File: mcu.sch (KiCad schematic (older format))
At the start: 11 parts

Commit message: Update schematic to KEMET and Panasonic passives.
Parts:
- removed C? (x3): CAP-EIA0402, footprints_generic:CAPC100X50X55L30N, symbol gz_Ceramic-Capacitors:CAP-EIA0402
- removed R?: RES-EIA0402, footprints_generic:RESC100X50X40L25NN, symbol gz_Chip-Resistors-Surface-Mount:RES-EIA0402
- added C? (x3): CAP-EIA0402, footprints_generic:CAPC100X50X55L30N, symbol gz_Ceramic-Capacitors:CAP-EIA0402
- added R?: RES-EIA0402, footprints_generic:RESC100X50X40L25NN, symbol gz_Chip-Resistors-Surface-Mount:RES-EIA0402
- C?: Dielectric X7R -> X5R; Digi-Key_PN 490-13341-1-ND -> (none); Fit (none) -> Yes; MPN GRM155R71E104ME14D -> C0402C104K4PACTU; Manufacturer Murata Electronics -> KEMET; Tolerance ±20% -> ±10%; Vendor (none) -> Digikey; Vendor_PN (none) -> 399-7762-1-ND; Voltage 25V -> 16V
- R?: Digi-Key_PN 541-4011-1-ND -> (none); Fit (none) -> Yes; MPN CRCW0402100KJNEDC -> ERJ-2GEJ104X; Manufacturer Vishay Dale -> Panasonic Electronic Components; Power 1/16W -> 1/10W; Vendor (none) -> Digikey; Vendor_PN (none) -> P100KJCT-ND; Voltage 50V -> N/A
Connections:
- net FLASH_MISO_IO1: now also R?.1
- net GND: now also C?.2, C?.2, C?.2, R?.2
- net at U?.26 (VDD_SDIO): now also C?.1
- net at U?.19 (VDD3P3_RTC), U?.37 (VDD3P3_CPU): now also C?.1, C?.1

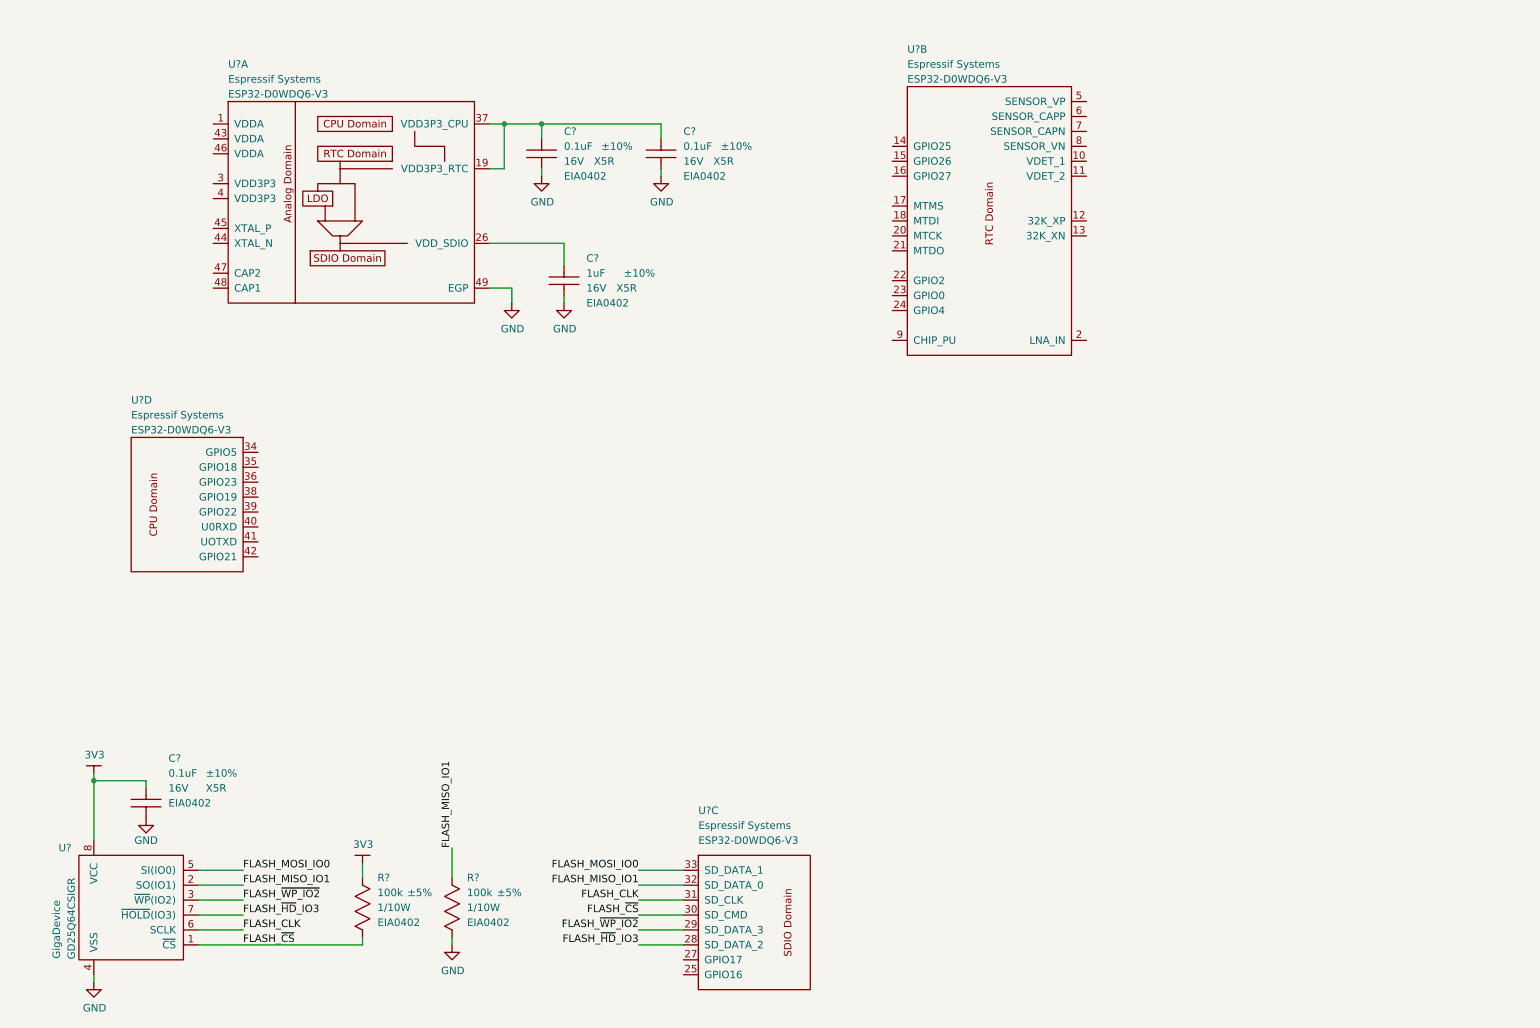
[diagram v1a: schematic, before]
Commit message: Add VDD3P3 pins decoupling and HF harmonics filter.
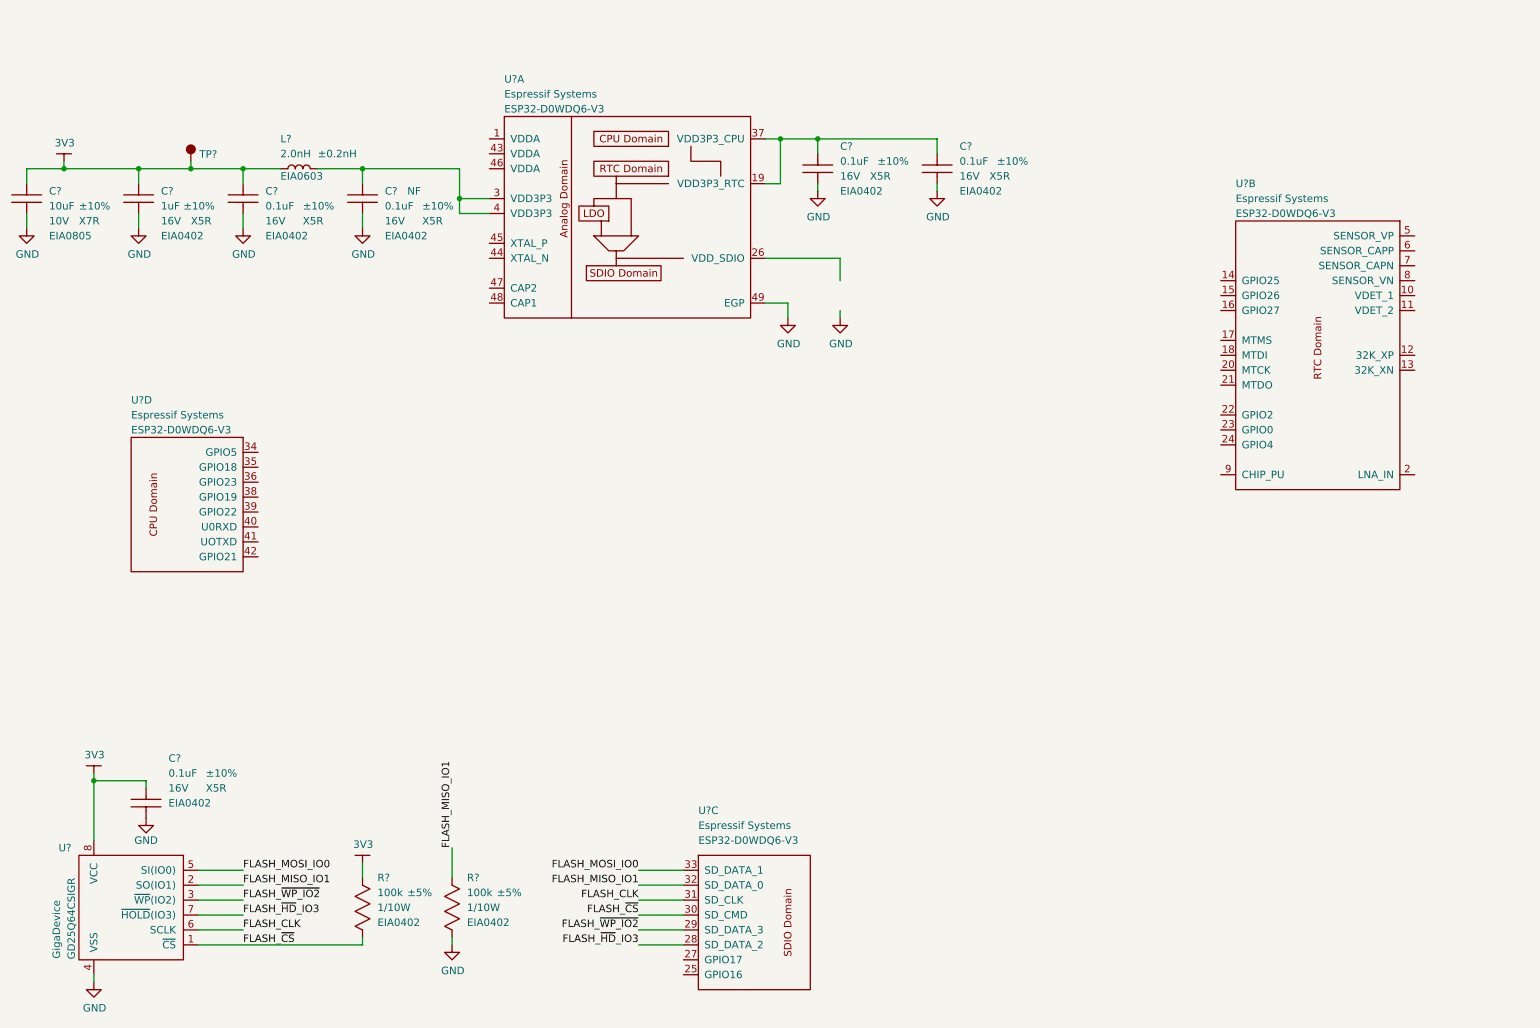
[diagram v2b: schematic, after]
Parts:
- added C? (x2): CAP-EIA0402, footprints_generic:CAPC100X50X55L30N, symbol gz_Ceramic-Capacitors:CAP-EIA0402
- added C?: CAP-EIA0805, footprints_generic:CAPC200X125X110L50N, symbol gz_Ceramic-Capacitors:CAP-EIA0805
- added L?: IND-EIA0603, footprints_generic:INDC160X80X95L40N, symbol gz_Fixed-Inductors:IND-EIA0603
- added TP?: Test-Point-SMT, footprints_generic:TestPoint-SMT_C100, symbol gz_Test-Points:Test-Point-SMT
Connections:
- wire segments 35 -> 56
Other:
- moved on the sheet: C?, U?A, U?B

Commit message: Sync repo, no change.
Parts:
- added C?: CAP-EIA0402, footprints_generic:CAPC100X50X55L30N, symbol gz_Ceramic-Capacitors:CAP-EIA0402
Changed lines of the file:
@@
-$Comp
-L gz_RF-Transceiver-ICs:Espressif_ESP32-D0WDQ6-V3 U?
-U 2 1 60500F62
-P 9350 2950
-F 0 "U?" H 8800 4000 50  0000 L CNN
-F 1 "Espressif_ESP32-D0WDQ6-V3" H 11100 4650 50  0001 L CNN
-F 2 "footprints:Espressif-ESP32_QFN49P40_600X600X90L40X20T430N" H 11100 4550 50  0001 L CNN
-F 3 "${DATASHEETS}/Espressif_ESP32-D0WDQ6-V3.pdf" H 10700 4250 50  0001 L CNN
-F 4 "1904-ESP32-D0WDQ6-V3CT-ND" H 11450 4450 50  0001 L CNN "Vendor_PN"
-F 5 "Espressif Systems" H 8800 3900 50  0000 L CNN "Manufacturer"
-F 6 "ESP32-D0WDQ6-V3" H 8800 3800 50  0000 L CNN "MPN"
-F 7 "RF/IF and RFID" H 11100 4350 50  0001 L CNN "Category"
-F 8 "RF Transceiver ICs" H 11100 4250 50  0001 L CNN "Family"
-F 9 "Yes" H 9100 3800 50  0001 L CNN "Fit"
-F 10 "Digikey" H 11100 4450 50  0001 L CNN "Vendor"
-	2    9350 2950
-	1    0    0    -1
-$EndComp
 $Comp
 L gz_RF-Transceiver-ICs:Espressif_ESP32-D0WDQ6-V3 U?
@@
 Wire Wire Line
 	1800 1800 1450 1800
+$Comp
+L gz_RF-Transceiver-ICs:Espressif_ESP32-D0WDQ6-V3 U?
+U 2 1 60500F62
+P 9350 2950
+F 0 "U?" H 8800 4000 50  0000 L CNN
+F 1 "Espressif_ESP32-D0WDQ6-V3" H 11100 4650 50  0001 L CNN
+F 2 "footprints:Espressif-ESP32_QFN49P40_600X600X90L40X20T430N" H 11100 4550 50  0001 L CNN
+F 3 "${DATASHEETS}/Espressif_ESP32-D0WDQ6-V3.pdf" H 10700 4250 50  0001 L CNN
+F 4 "1904-ESP32-D0WDQ6-V3CT-ND" H 11450 4450 50  0001 L CNN "Vendor_PN"
+F 5 "Espressif Systems" H 8800 3900 50  0000 L CNN "Manufacturer"
+F 6 "ESP32-D0WDQ6-V3" H 8800 3800 50  0000 L CNN "MPN"
+F 7 "RF/IF and RFID" H 11100 4350 50  0001 L CNN "Category"
+F 8 "RF Transceiver ICs" H 11100 4250 50  0001 L CNN "Family"
+F 9 "Yes" H 9100 3800 50  0001 L CNN "Fit"
+F 10 "Digikey" H 11100 4450 50  0001 L CNN "Vendor"
+	2    9350 2950
+	1    0    0    -1
+$EndComp
+$Comp
+L gz_Ceramic-Capacitors:CAP-EIA0402 C?
+U 1 1 60517A0C
+P 6150 2650
+F 0 "C?" V 6100 2800 50  0000 L CNN
+F 1 "CAP-EIA0402" H 6550 3750 50  0001 L CNN
+F 2 "footprints_generic:CAPC100X50X55L30N" H 2850 7000 50  0001 L CNN
+F 3 "${KEMET_MLCC_BASE}C0402C105K4PACTU" H 2850 7100 50  0001 L CNN
+F 4 "Digikey" H 6150 2650 50  0001 L CNN "Vendor"
+F 5 "399-12289-1-ND" H 6150 2650 50  0001 L CNN "Vendor_PN"
+F 6 "KEMET" H 6550 3550 50  0001 L CNN "Manufacturer"
+F 7 "C0402C105K4PACTU" H 6550 3450 50  0001 L CNN "MPN"
+F 8 "Capacitors" H 2850 7400 50  0001 L CNN "Category"
+F 9 "Ceramic Capacitors" H 2850 7500 50  0001 L CNN "Family"
+F 10 "Yes" H 6150 2650 50  0001 L CNN "Fit"
+F 11 "1uF" V 6200 2800 50  0000 L CNN "Capacitance"
+F 12 "±10%" V 6200 2950 50  0000 L CNN "Tolerance"
+F 13 "16V" V 6300 2800 50  0000 L CNN "Voltage"
+F 14 "X5R" V 6300 3000 50  0000 L CNN "Dielectric"
+F 15 "EIA0402" V 6400 2800 50  0000 L CNN "Package"
+	1    6150 2650
+	0    1    1    0
+$EndComp
 $EndSCHEMATC

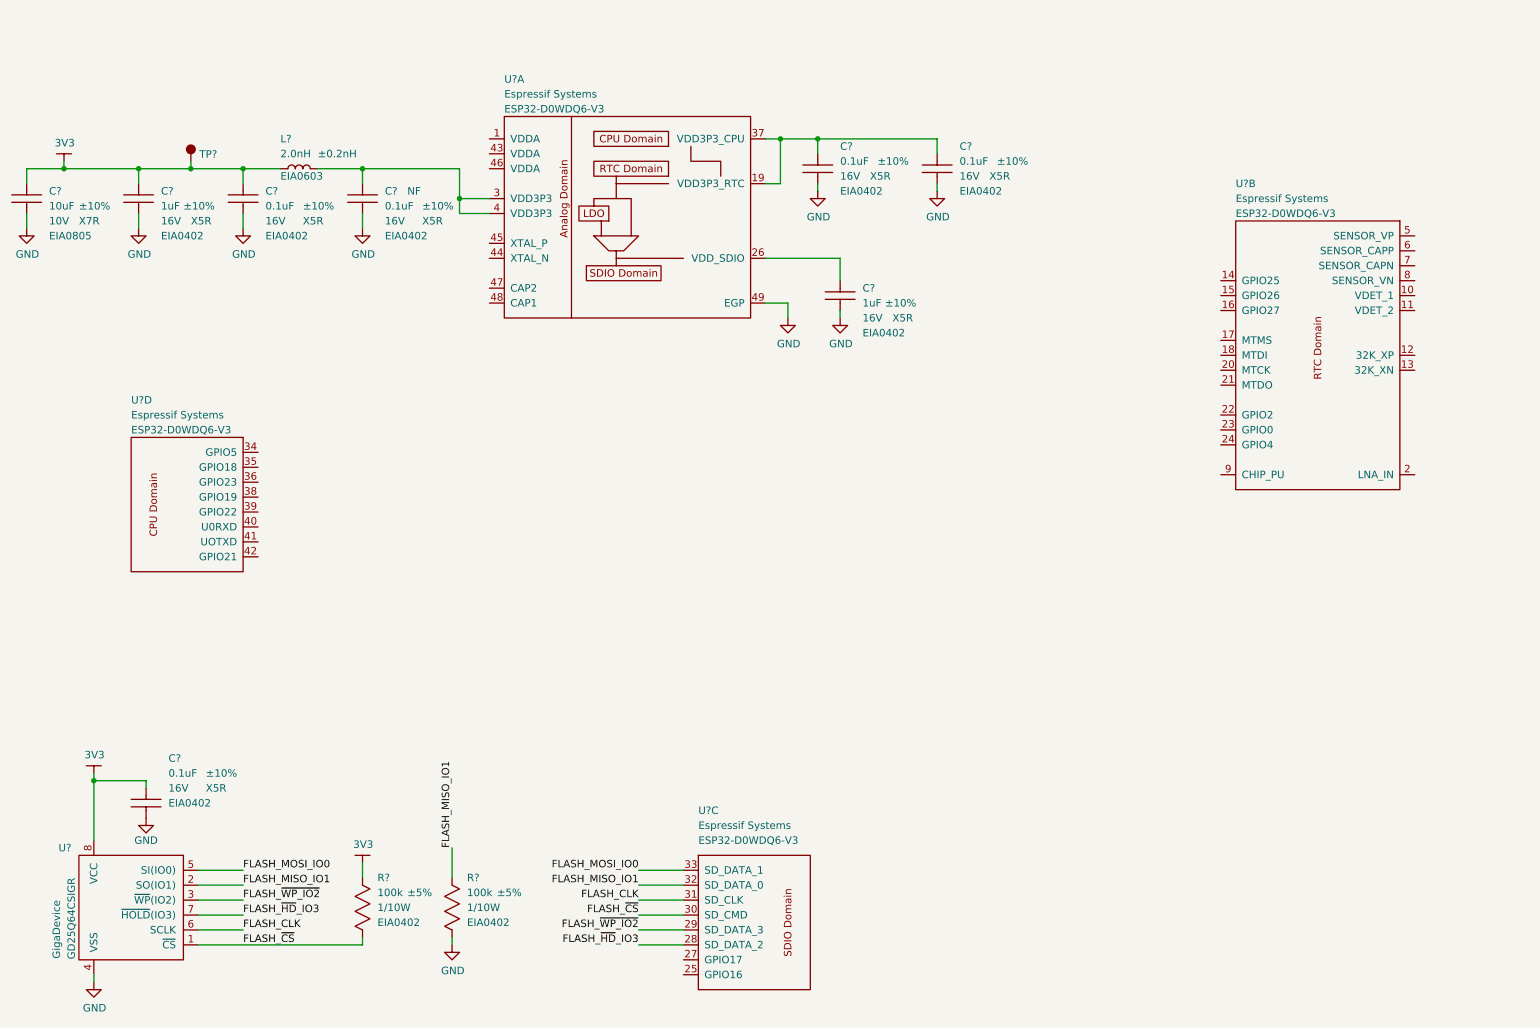
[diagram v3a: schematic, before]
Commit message: Conclude PSU section of ESP32.
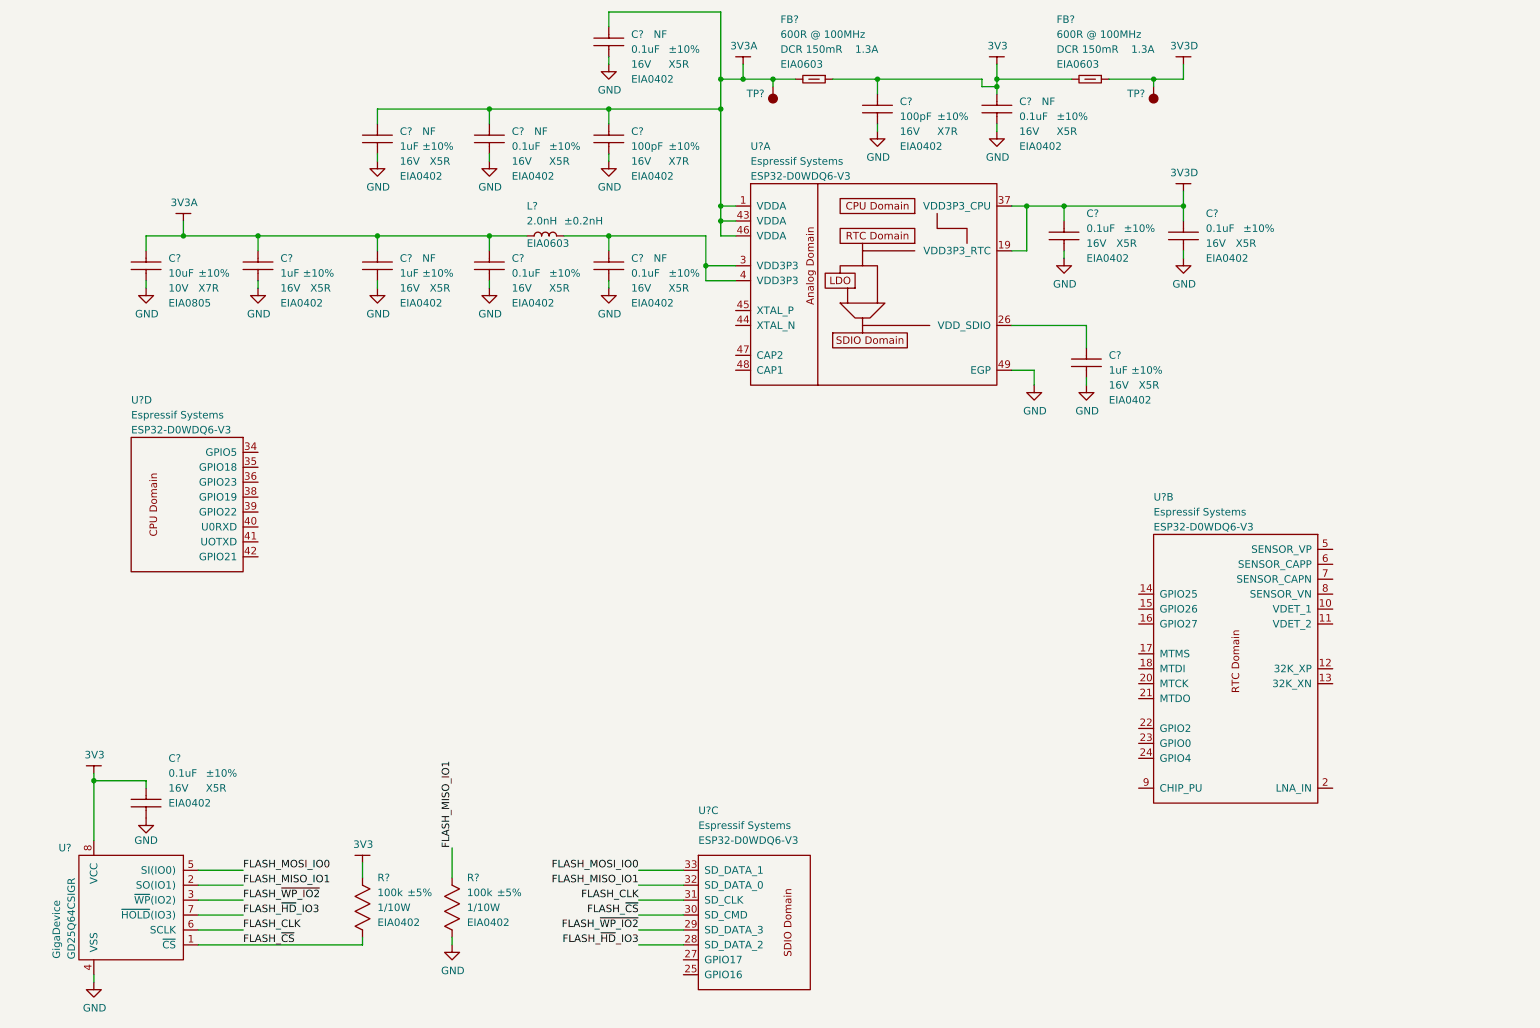
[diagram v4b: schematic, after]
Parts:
- added C? (x7): CAP-EIA0402, footprints_generic:CAPC100X50X55L30N, symbol gz_Ceramic-Capacitors:CAP-EIA0402
- added FB? (x2): FB-EIA0603, footprints_generic:BEADC160X80X95L40N, symbol gz_Ferrite-Beads-and-Chips:FB-EIA0603
- added TP?: Test-Point-SMT, footprints_generic:TestPoint-SMT_C100, symbol gz_Test-Points:Test-Point-SMT
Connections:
- net +3V3: now also C?.1, C?.1, U?.1 (VDDA), U?.19 (VDD3P3_RTC), U?.37 (VDD3P3_CPU), U?.43 (VDDA), U?.46 (VDDA), C?.1, C?.1, C?.1, C?.1, C?.1, C?.1, C?.1, FB?.1, FB?.1, FB?.2, FB?.2, TP?.1
- net GND: now also C?.2, C?.2, C?.2, C?.2, C?.2, C?.2, C?.2
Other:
- moved on the sheet: C?, L?, U?A, U?B

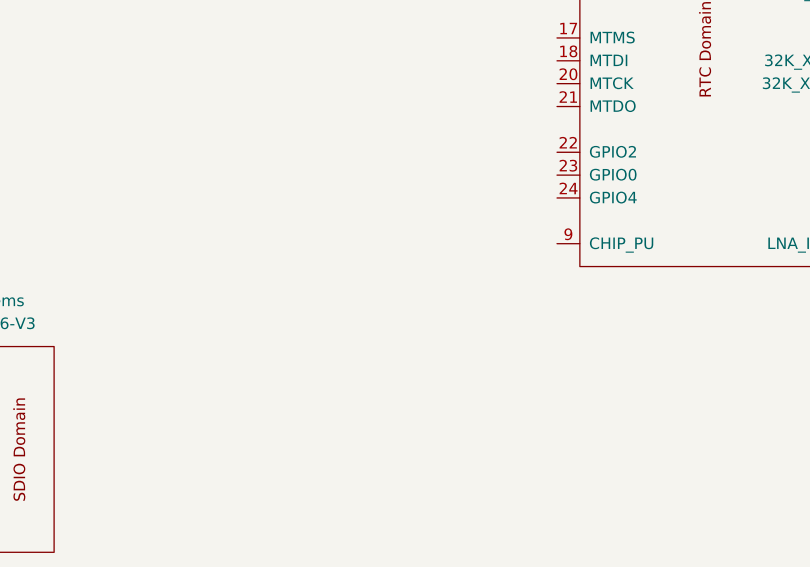
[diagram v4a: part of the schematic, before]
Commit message: Add ESP32 reset line R.
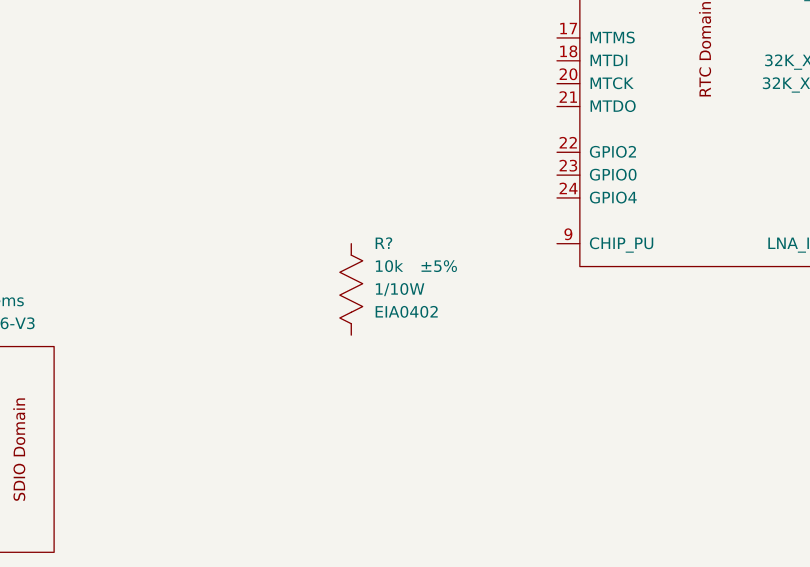
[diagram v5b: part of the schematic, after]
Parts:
- added R?: RES-EIA0402, footprints_generic:RESC100X50X40L25NN, symbol gz_Chip-Resistors-Surface-Mount:RES-EIA0402
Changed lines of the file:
@@
 Wire Wire Line
 	8250 1200 8450 1200
+$Comp
+L gz_Chip-Resistors-Surface-Mount:RES-EIA0402 R?
+U 1 1 605F571C
+P 7250 6150
+F 0 "R?" V 7050 6250 50  0000 L CNN
+F 1 "RES-EIA0402" H 8050 7050 50  0001 L CNN
+F 2 "footprints_generic:RESC100X50X40L25NN" H 3950 10500 50  0001 L CNN
+F 3 "${PANASONIC_GP_CHIP_RES_BASE}ERJ2GEJ103X" H 3950 10600 50  0001 L CNN
+F 4 "Digikey" H 7250 6150 50  0001 L CNN "Vendor"
+F 5 "P10KJCT-ND" H 7250 6150 50  0001 L CNN "Vendor_PN"
+F 6 "Panasonic Electronic Components" H 8050 6850 50  0001 L CNN "Manufacturer"
+F 7 "ERJ2GEJ103X" H 8050 6750 50  0001 L CNN "MPN"
+F 8 "Resistors" H 3950 10900 50  0001 L CNN "Category"
+F 9 "Chip Resistor - Surface Mount" H 3950 11000 50  0001 L CNN "Family"
+F 10 "Yes" H 7250 6150 50  0001 C CNN "Fit"
+F 11 "10k" V 7150 6250 50  0000 L CNN "Resistance"
+F 12 "±5%" V 7150 6450 50  0000 L CNN "Tolerance"
+F 13 "1/10W" V 7250 6250 50  0000 L CNN "Power"
+F 14 "N/A" H 7250 6365 50  0001 L CNN "Voltage"
+F 15 "EIA0402" V 7350 6250 50  0000 L CNN "Package"
+	1    7250 6150
+	0    1    1    0
+$EndComp
 $EndSCHEMATC
